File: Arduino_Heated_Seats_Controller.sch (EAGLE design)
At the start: 23 parts, among them U1 MEGA8-AI, U2 UA78M05CDCY, U3 ULN2003ADE4, U4 IC_TD62783-SO-18W

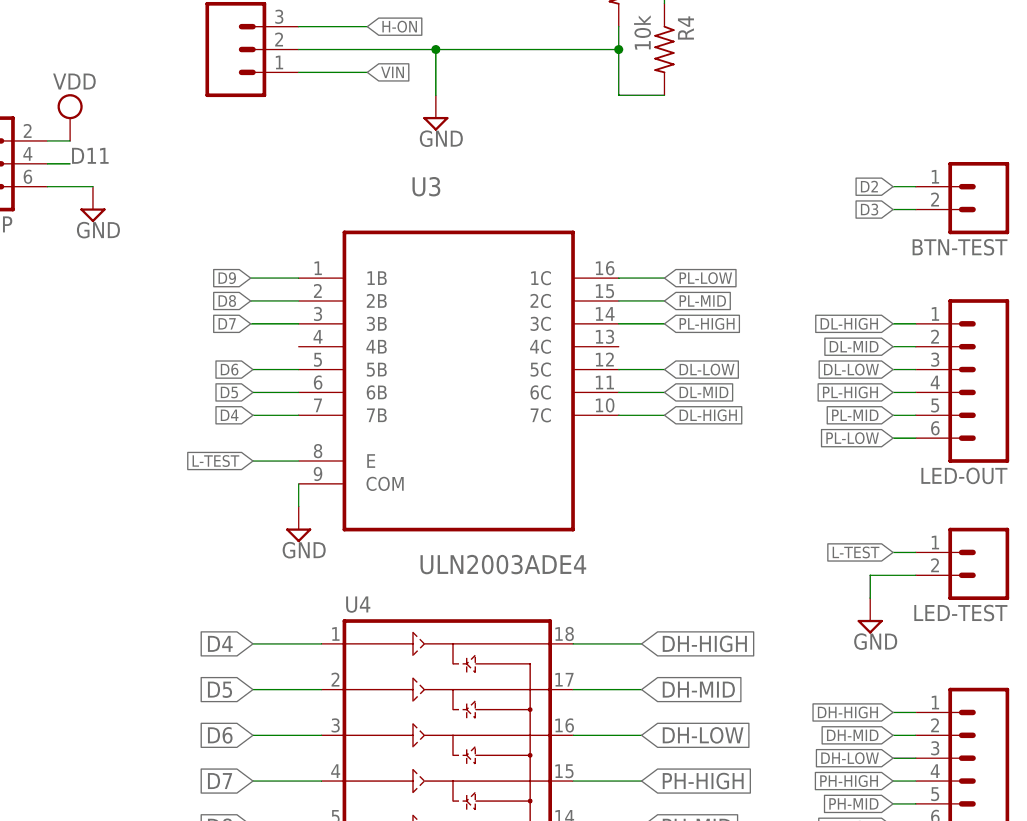
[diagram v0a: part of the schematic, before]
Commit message: Changes: Removed test pins.
Corrections:
Removed ground on ULN2003A pin 9.
GND on ULN2003A is pin 8 (pin 9 is COMMON/E).
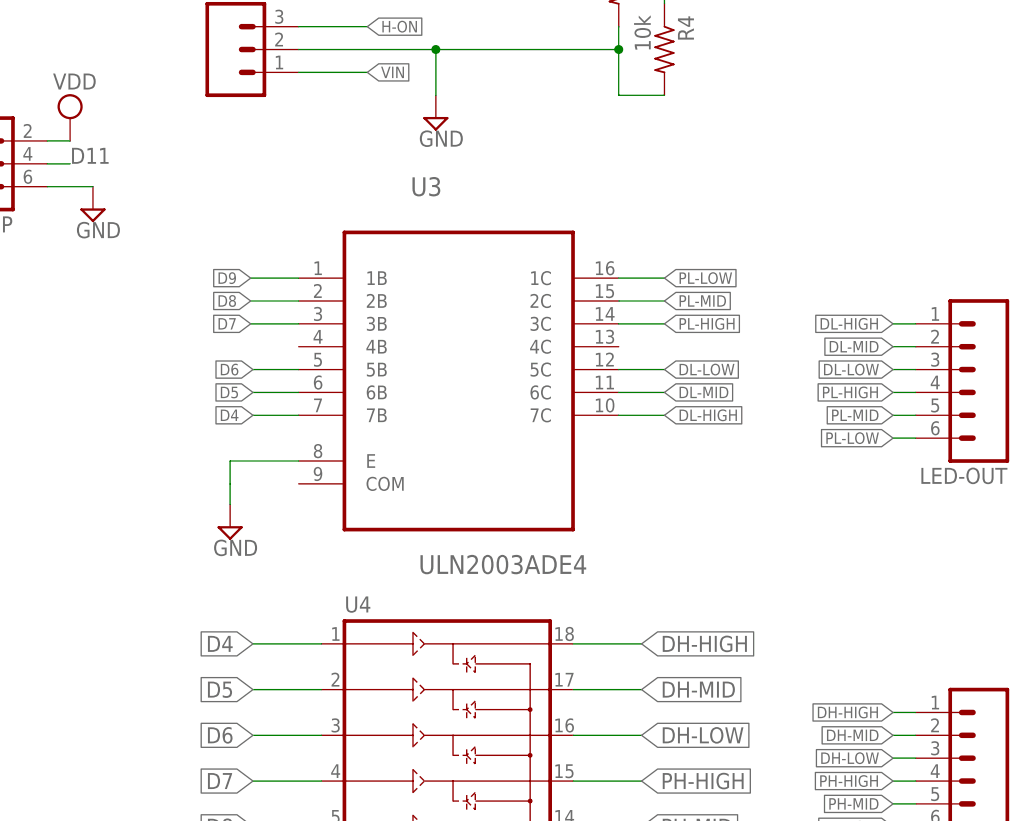
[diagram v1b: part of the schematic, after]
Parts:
- removed BTN-TEST, LED-TEST: M02PTH, SparkFun-Connectors:M02PTH
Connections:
- removed net L-TEST: LED-TEST.1, U3.E
- net D2: no longer BTN-TEST.1
- net D3: no longer BTN-TEST.2
- net GND: now also U3.E; no longer LED-TEST.2, U3.COM
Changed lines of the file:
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@@
 <part name="LED-OUT" library="SparkFun-Connectors" deviceset="M06" device="SIP"/>
 <part name="H-OUT" library="SparkFun-Connectors" deviceset="M06" device="SIP"/>
-<part name="LED-TEST" library="SparkFun-Connectors" deviceset="M02" device="PTH" value=""/>
-<part name="BTN-TEST" library="SparkFun-Connectors" deviceset="M02" device="PTH" value=""/>
 <part name="U1" library="atmel" deviceset="MEGA8" device="-AI"/>
 <part name="SUPPLY1" library="supply2" deviceset="GND" device=""/>
@@
 <part name="SUPPLY12" library="supply2" deviceset="GND" device=""/>
 <part name="SUPPLY17" library="supply2" deviceset="GND" device=""/>
-<part name="SUPPLY19" library="supply2" deviceset="GND" device=""/>
 <part name="R1" library="resistor" deviceset="R-US_" device="R0603" value="15k"/>
 <part name="R2" library="resistor" deviceset="R-US_" device="R0603" value="15k"/>
@@
 <instance part="LED-OUT" gate="G$1" x="213.36" y="81.28" rot="R180"/>
 <instance part="H-OUT" gate="G$1" x="213.36" y="38.1" rot="R180"/>
-<instance part="LED-TEST" gate="G$1" x="215.9" y="60.96" rot="R180"/>
-<instance part="BTN-TEST" gate="G$1" x="215.9" y="101.6" rot="R180"/>
 <instance part="U1" gate="G$1" x="68.58" y="63.5"/>
 <instance part="SUPPLY1" gate="GND" x="20.32" y="66.04"/>
@@
 <instance part="SUPPLY16" gate="GND" x="116.84" y="99.06"/>
 <instance part="SUPPLY12" gate="GND" x="154.94" y="109.22"/>
-<instance part="SUPPLY17" gate="GND" x="139.7" y="63.5"/>
-<instance part="SUPPLY19" gate="GND" x="203.2" y="53.34"/>
+<instance part="SUPPLY17" gate="GND" x="132.08" y="63.754"/>
 <instance part="R1" gate="G$1" x="157.48" y="132.08"/>
 <instance part="R2" gate="G$1" x="167.64" y="134.62"/>
@@
 <net name="GND" class="0">
 <segment>
-<pinref part="SUPPLY17" gate="GND" pin="GND"/>
-<pinref part="U3" gate="A" pin="COM"/>
-<wire x1="139.7" y1="68.58" x2="139.7" y2="66.04" width="0.1524" layer="91"/>
-</segment>
-<segment>
-<pinref part="LED-TEST" gate="G$1" pin="2"/>
-<wire x1="208.28" y1="58.42" x2="203.2" y2="58.42" width="0.1524" layer="91"/>
-<wire x1="203.2" y1="58.42" x2="203.2" y2="55.88" width="0.1524" layer="91"/>
-<pinref part="SUPPLY19" gate="GND" pin="GND"/>
-</segment>
-<segment>
 <wire x1="154.94" y1="111.76" x2="154.94" y2="116.84" width="0.1524" layer="91"/>
 <wire x1="180.34" y1="111.76" x2="175.26" y2="111.76" width="0.1524" layer="91"/>
@@
 <junction x="27.94" y="114.3"/>
 </segment>
+<segment>
+<pinref part="SUPPLY17" gate="GND" pin="GND"/>
+<wire x1="132.08" y1="66.294" x2="132.08" y2="68.58" width="0.1524" layer="91"/>
+<pinref part="U3" gate="A" pin="E"/>
+<wire x1="139.7" y1="71.12" x2="132.08" y2="71.12" width="0.1524" layer="91"/>
+<wire x1="132.08" y1="68.58" x2="132.08" y2="71.12" width="0.1524" layer="91"/>
+</segment>
 </net>
 <net name="D2" class="0">
@@
 </segment>
 <segment>
-<pinref part="BTN-TEST" gate="G$1" pin="1"/>
-<wire x1="208.28" y1="101.6" x2="205.74" y2="101.6" width="0.1524" layer="91"/>
-<label x="205.74" y="101.6" size="1.27" layer="95" rot="R180" xref="yes"/>
-</segment>
-<segment>
 <wire x1="93.98" y1="60.96" x2="96.52" y2="60.96" width="0.1524" layer="91"/>
 <label x="96.52" y="60.96" size="1.778" layer="95"/>
@@
 <pinref part="R2" gate="G$1" pin="2"/>
 <pinref part="R4" gate="G$1" pin="1"/>
-</segment>
-<segment>
-<pinref part="BTN-TEST" gate="G$1" pin="2"/>
-<wire x1="208.28" y1="99.06" x2="205.74" y2="99.06" width="0.1524" layer="91"/>
-<label x="205.74" y="99.06" size="1.27" layer="95" rot="R180" xref="yes"/>
 </segment>
 <segment>
@@
 </segment>
 </net>
-<net name="L-TEST" class="0">
-<segment>
-<wire x1="139.7" y1="71.12" x2="134.62" y2="71.12" width="0.1524" layer="91"/>
-<label x="134.62" y="71.12" size="1.27" layer="95" rot="R180" xref="yes"/>
-<pinref part="U3" gate="A" pin="E"/>
-</segment>
-<segment>
-<pinref part="LED-TEST" gate="G$1" pin="1"/>
-<wire x1="208.28" y1="60.96" x2="205.74" y2="60.96" width="0.1524" layer="91"/>
-<label x="205.74" y="60.96" size="1.27" layer="95" rot="R180" xref="yes"/>
-</segment>
-</net>
